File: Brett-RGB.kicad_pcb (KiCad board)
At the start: 2 copper layers, 223 x 73.5 mm, 195 parts, among them P1 USB_OTG, P2 CONN_01X04, P3 CONN_01X05, P4 FLASH_HDR, P5 CONN_01X04, P6 CONN_01X02, P7 CONN_01X02, SW1 SW_PUSH, SW10 SW_PUSH, SW11 SW_PUSH, SW12 SW_PUSH, SW13 SW_PUSH, SW14 SW_PUSH, SW15 SW_PUSH, SW16 SW_PUSH, SW17 SW_PUSH, SW18 SW_PUSH, SW19 SW_PUSH, SW2 SW_PUSH, SW20 SW_PUSH, SW21 SW_PUSH, SW22 SW_PUSH, SW23 SW_PUSH, SW24 SW_PUSH, SW25 SW_PUSH, SW26 SW_PUSH, SW27 SW_PUSH, SW28 SW_PUSH, SW29 SW_PUSH, SW3 SW_PUSH, SW30 SW_PUSH, SW31 SW_PUSH, SW32 SW_PUSH, SW33 SW_PUSH, SW34 SW_PUSH, SW35 SW_PUSH, SW36 SW_PUSH, SW37 SW_PUSH, SW38 SW_PUSH, SW39 SW_PUSH, SW4 SW_PUSH, SW40 SW_PUSH, SW41 SW_PUSH, SW42 SW_PUSH, SW43 SW_PUSH, SW44 SW_PUSH, SW45 SW_PUSH, SW46 SW_PUSH, SW47 SW_PUSH, SW48 TAC_SWITCH, SW5 SW_PUSH, SW6 SW_PUSH, SW7 SW_PUSH, SW8 SW_PUSH, SW9 SW_PUSH, U1 IS31FL3737, U2 MK20DX256VLH7-RESCUE-RainbowF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, X1 CRYSTAL_SMD

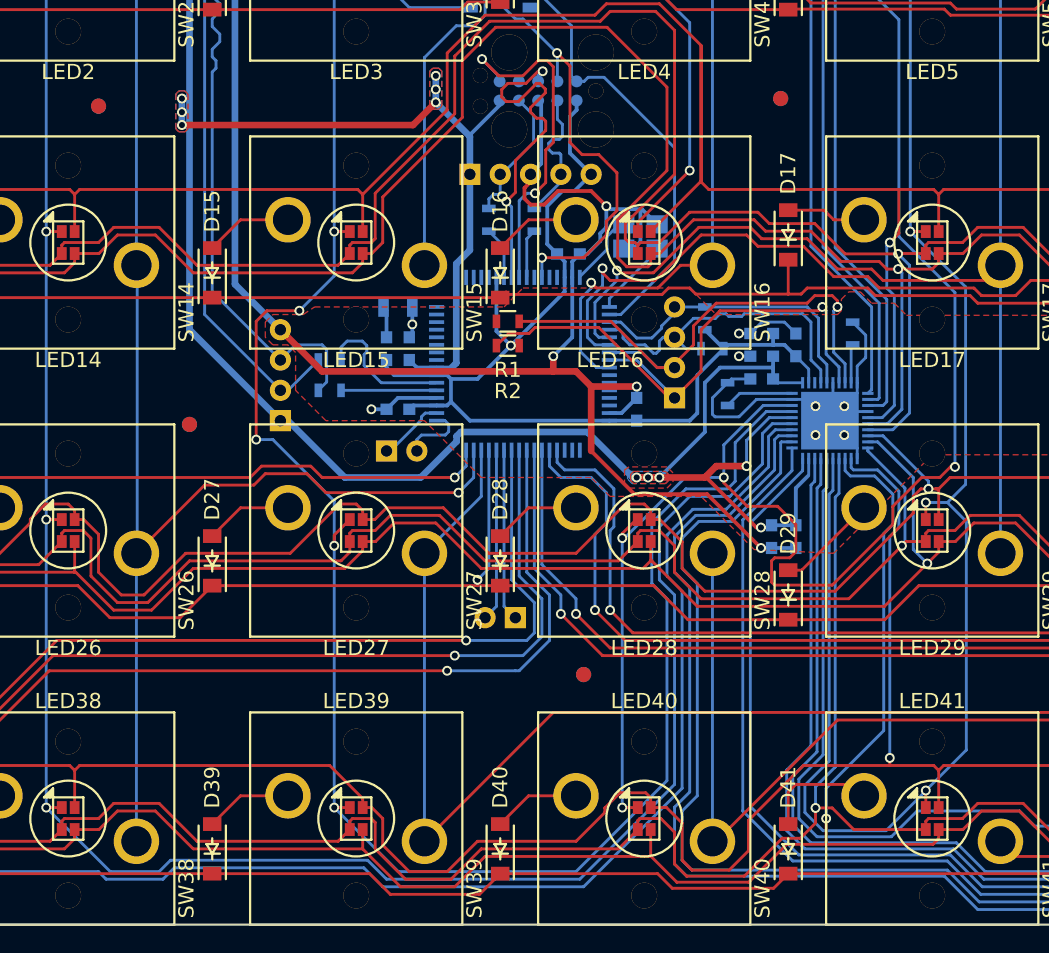
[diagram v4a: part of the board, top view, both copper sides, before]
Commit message: Fixed MCU name in Schematic
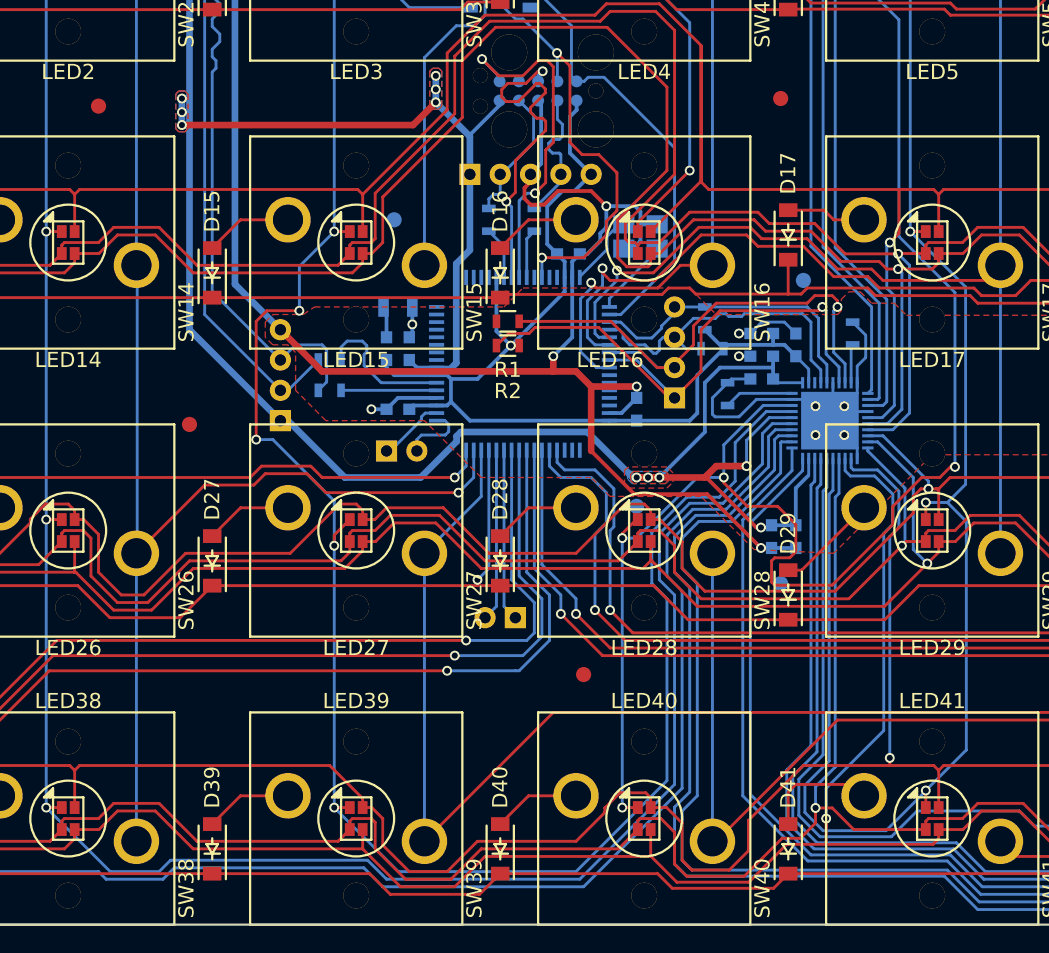
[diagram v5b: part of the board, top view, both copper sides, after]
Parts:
- moved ? 30.0 mm to (101.5, 78.4)
- moved ? 20.9 mm to (85.5, 59.5)
- moved ? 14.3 mm to (111.0, 83.5)
- moved ? 12.1 mm to (112.5, 63.5)
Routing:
- net /CS6: track 200.8 -> 200.2 mm
